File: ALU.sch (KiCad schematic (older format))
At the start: 34 parts, among them U37 74LS245, U38 74LS00, U39 74LS86, U40 74LS86, U41 74LS86, U42 74LS00, U43 74LS86, U44 74HC02, U45 74LS00, U46 74LS00, U47 74LS283, U48 74LS85, U49 74LS283, U50 74LS245, U51 74LS85, U52 74LS245, U53 74LS283, U54 74LS85, U55 74LS173, U56 74LS283, U57 74LS245, U58 74LS85

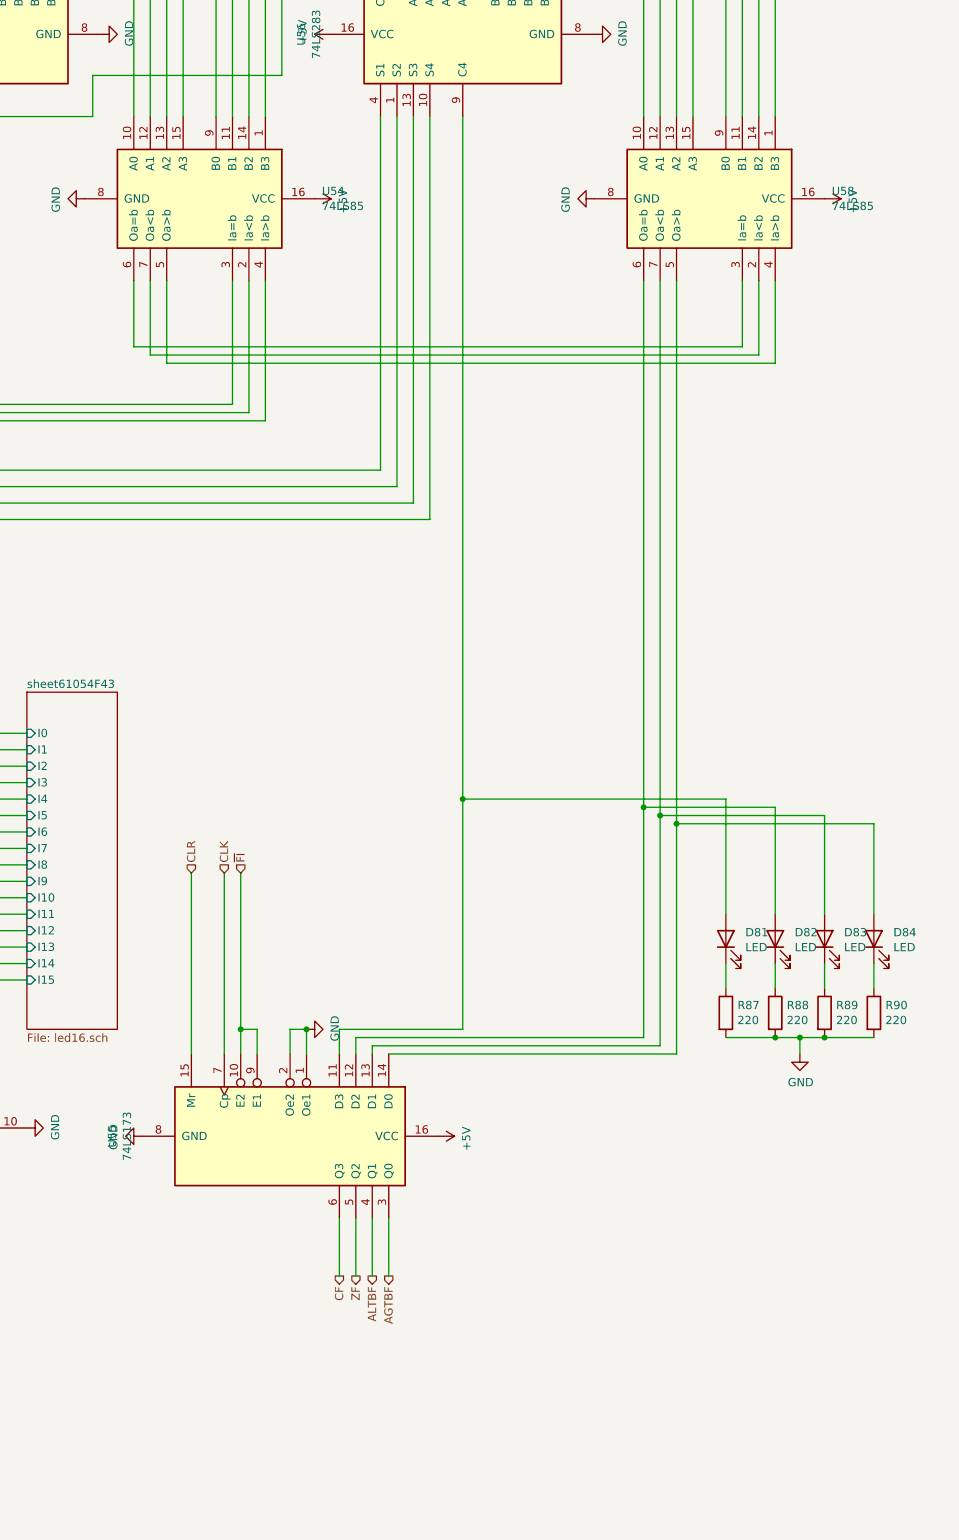
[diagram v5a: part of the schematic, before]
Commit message: added swp_x, and cleanup readme
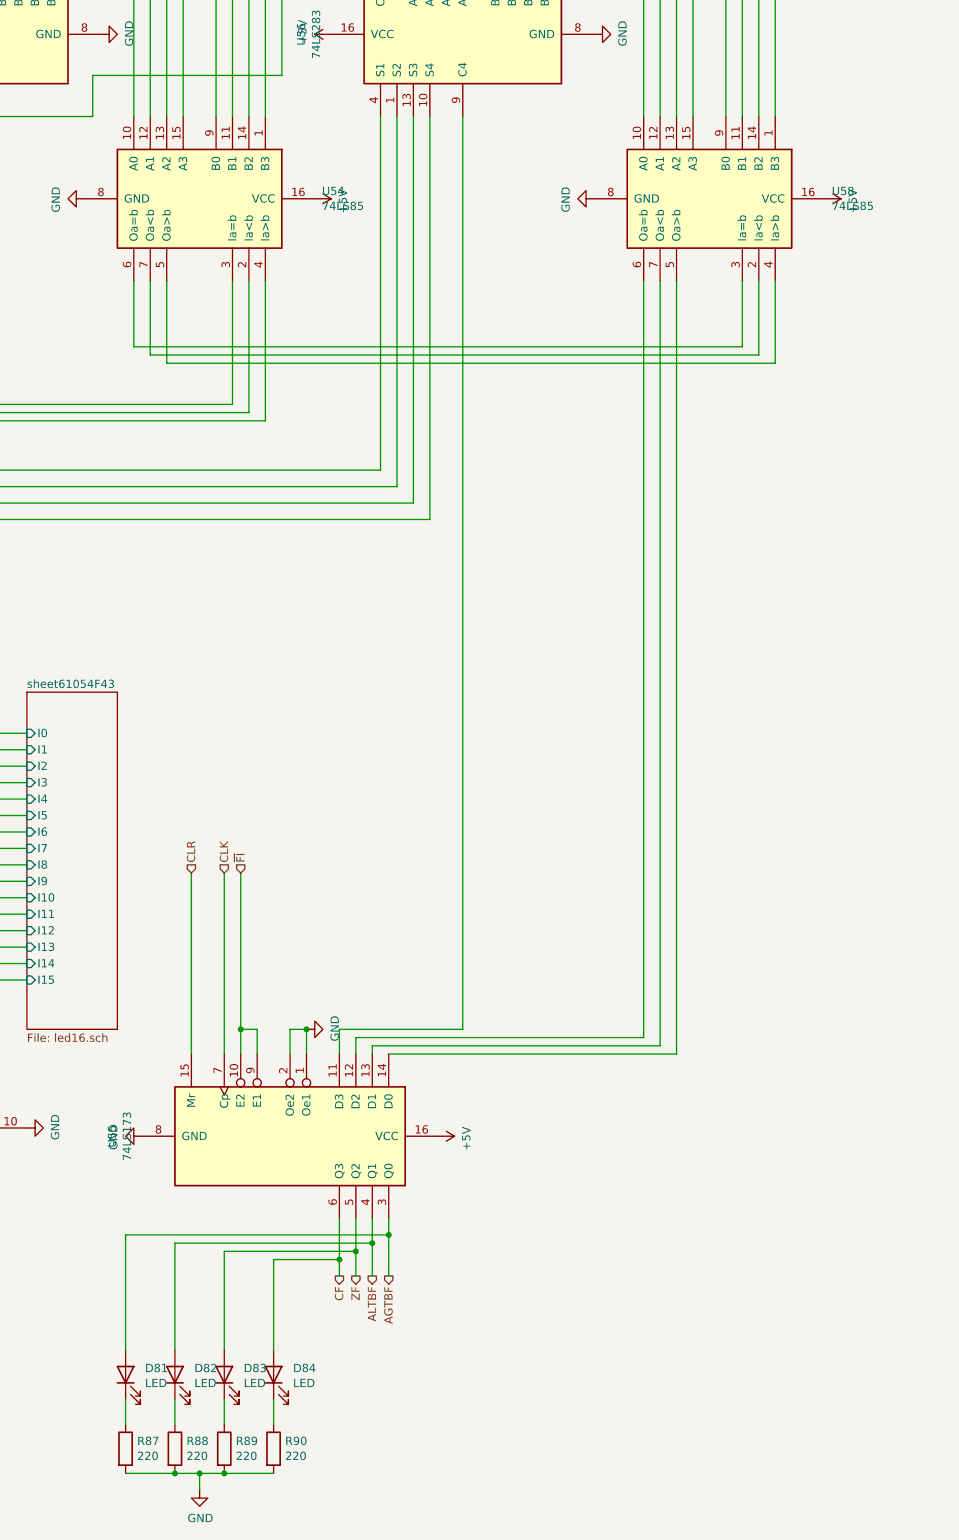
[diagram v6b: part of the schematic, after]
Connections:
- net AGTBF: now also D81.2 (A)
- net ALTBF: now also D82.2 (A)
- net CF: now also D84.2 (A)
- net ZF: now also D83.2 (A)
- net at U55.11 (D3), U56.9 (C4): no longer D81.2 (A)
- net at U55.12 (D2), U58.6 (Oa=b): no longer D82.2 (A)
- net at U55.13 (D1), U58.7 (Oa<b): no longer D83.2 (A)
- net at U55.14 (D0), U58.5 (Oa>b): no longer D84.2 (A)
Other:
- moved on the sheet: D81, D82, D83, D84, R87, R88, R89, R90
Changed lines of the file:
@@
 	17900 17350 19650 17350
 Wire Wire Line
-	19550 12650 19550 15900
-Wire Wire Line
 	19550 17300 17800 17300
 Wire Wire Line
@@
 Wire Wire Line
 	17700 17250 19450 17250
-Wire Wire Line
-	19450 17250 19450 15850
-Wire Wire Line
-	18350 11650 18350 15800
 Wire Wire Line
 	18350 17200 17600 17200
@@
 L Device:LED D?
 U 1 1 6367F2BC
-P 20250 16650
+P 16600 19300
 AR Path="/5F926C74/6367F2BC" Ref="D?"  Part="1"
 AR Path="/61968B9B/60C9B37A/6367F2BC" Ref="D?"  Part="1"
@@
 AR Path="/5FD099BF/625B6FDA/6367F2BC" Ref="D?"  Part="1"
 AR Path="/5F5F4A69/6367F2BC" Ref="D82"  Part="1"
-F 0 "D82" V 20289 16532 50  0000 R CNN
-F 1 "LED" V 20198 16532 50  0000 R CNN
-F 2 "LED_THT:LED_D3.0mm" H 20250 16650 50  0001 C CNN
-F 3 "" H 20250 16650 50  0001 C CNN
-	1    20250 16650
+F 0 "D82" V 16639 19182 50  0000 R CNN
+F 1 "LED" V 16548 19182 50  0000 R CNN
+F 2 "LED_THT:LED_D3.0mm" H 16600 19300 50  0001 C CNN
+F 3 "" H 16600 19300 50  0001 C CNN
+	1    16600 19300
 	0    -1   -1   0
 $EndComp
@@
 L Device:LED D?
 U 1 1 6367F2C2
-P 20550 16650
+P 16900 19300
 AR Path="/5F926C74/6367F2C2" Ref="D?"  Part="1"
 AR Path="/61968B9B/60C9B37A/6367F2C2" Ref="D?"  Part="1"
@@
 AR Path="/5FD099BF/625B6FDA/6367F2C2" Ref="D?"  Part="1"
 AR Path="/5F5F4A69/6367F2C2" Ref="D83"  Part="1"
-F 0 "D83" V 20589 16532 50  0000 R CNN
-F 1 "LED" V 20498 16532 50  0000 R CNN
-F 2 "LED_THT:LED_D3.0mm" H 20550 16650 50  0001 C CNN
-F 3 "" H 20550 16650 50  0001 C CNN
-	1    20550 16650
+F 0 "D83" V 16939 19182 50  0000 R CNN
+F 1 "LED" V 16848 19182 50  0000 R CNN
+F 2 "LED_THT:LED_D3.0mm" H 16900 19300 50  0001 C CNN
+F 3 "" H 16900 19300 50  0001 C CNN
+	1    16900 19300
 	0    -1   -1   0
 $EndComp
@@
 L Device:LED D?
 U 1 1 6367F2C8
-P 20850 16650
+P 17200 19300
 AR Path="/5F926C74/6367F2C8" Ref="D?"  Part="1"
 AR Path="/61968B9B/60C9B37A/6367F2C8" Ref="D?"  Part="1"
@@
 AR Path="/5FD099BF/625B6FDA/6367F2C8" Ref="D?"  Part="1"
 AR Path="/5F5F4A69/6367F2C8" Ref="D84"  Part="1"
-F 0 "D84" V 20889 16532 50  0000 R CNN
-F 1 "LED" V 20798 16532 50  0000 R CNN
-F 2 "LED_THT:LED_D3.0mm" H 20850 16650 50  0001 C CNN
-F 3 "" H 20850 16650 50  0001 C CNN
-	1    20850 16650
+F 0 "D84" V 17239 19182 50  0000 R CNN
+F 1 "LED" V 17148 19182 50  0000 R CNN
+F 2 "LED_THT:LED_D3.0mm" H 17200 19300 50  0001 C CNN
+F 3 "" H 17200 19300 50  0001 C CNN
+	1    17200 19300
 	0    -1   -1   0
 $EndComp
 Wire Wire Line
-	20250 16800 20250 16950
-Wire Wire Line
-	20550 16800 20550 16950
-Wire Wire Line
-	20850 16800 20850 16950
+	16600 19450 16600 19600
+Wire Wire Line
+	16900 19450 16900 19600
+Wire Wire Line
+	17200 19450 17200 19600
 $Comp
 L Device:R R?
 U 1 1 6367F2D7
-P 20250 17100
+P 16600 19750
 AR Path="/5F926C74/6367F2D7" Ref="R?"  Part="1"
 AR Path="/61968B9B/60C9B37A/6367F2D7" Ref="R?"  Part="1"
@@
 AR Path="/5FD099BF/625B6FDA/6367F2D7" Ref="R?"  Part="1"
 AR Path="/5F5F4A69/6367F2D7" Ref="R88"  Part="1"
-F 0 "R88" H 20320 17146 50  0000 L CNN
-F 1 "220" H 20320 17055 50  0000 L CNN
-F 2 "Resistor_THT:R_Axial_DIN0204_L3.6mm_D1.6mm_P7.62mm_Horizontal" V 20180 17100 50  0001 C CNN
-F 3 "" H 20250 17100 50  0001 C CNN
-	1    20250 17100
+F 0 "R88" H 16670 19796 50  0000 L CNN
+F 1 "220" H 16670 19705 50  0000 L CNN
+F 2 "Resistor_THT:R_Axial_DIN0204_L3.6mm_D1.6mm_P7.62mm_Horizontal" V 16530 19750 50  0001 C CNN
+F 3 "" H 16600 19750 50  0001 C CNN
+	1    16600 19750
 	1    0    0    -1
 $EndComp
@@
 L Device:R R?
 U 1 1 6367F2DD
-P 20550 17100
+P 16900 19750
 AR Path="/5F926C74/6367F2DD" Ref="R?"  Part="1"
 AR Path="/61968B9B/60C9B37A/6367F2DD" Ref="R?"  Part="1"
@@
 AR Path="/5FD099BF/625B6FDA/6367F2DD" Ref="R?"  Part="1"
 AR Path="/5F5F4A69/6367F2DD" Ref="R89"  Part="1"
-F 0 "R89" H 20620 17146 50  0000 L CNN
-F 1 "220" H 20620 17055 50  0000 L CNN
-F 2 "Resistor_THT:R_Axial_DIN0204_L3.6mm_D1.6mm_P7.62mm_Horizontal" V 20480 17100 50  0001 C CNN
-F 3 "" H 20550 17100 50  0001 C CNN
-	1    20550 17100
+F 0 "R89" H 16970 19796 50  0000 L CNN
+F 1 "220" H 16970 19705 50  0000 L CNN
+F 2 "Resistor_THT:R_Axial_DIN0204_L3.6mm_D1.6mm_P7.62mm_Horizontal" V 16830 19750 50  0001 C CNN
+F 3 "" H 16900 19750 50  0001 C CNN
+	1    16900 19750
 	1    0    0    -1
 $EndComp
@@
 L Device:R R?
 U 1 1 6367F2E3
-P 20850 17100
+P 17200 19750
 AR Path="/5F926C74/6367F2E3" Ref="R?"  Part="1"
 AR Path="/61968B9B/60C9B37A/6367F2E3" Ref="R?"  Part="1"
@@
 AR Path="/5FD099BF/625B6FDA/6367F2E3" Ref="R?"  Part="1"
 AR Path="/5F5F4A69/6367F2E3" Ref="R90"  Part="1"
-F 0 "R90" H 20920 17146 50  0000 L CNN
-F 1 "220" H 20920 17055 50  0000 L CNN
-F 2 "Resistor_THT:R_Axial_DIN0204_L3.6mm_D1.6mm_P7.62mm_Horizontal" V 20780 17100 50  0001 C CNN
-F 3 "" H 20850 17100 50  0001 C CNN
-	1    20850 17100
-	1    0    0    -1
-$EndComp
-Wire Wire Line
-	19950 17250 20250 17250
-Connection ~ 20250 17250
-Wire Wire Line
-	20250 17250 20400 17250
-Connection ~ 20550 17250
-Wire Wire Line
-	20550 17250 20850 17250
+F 0 "R90" H 17270 19796 50  0000 L CNN
+F 1 "220" H 17270 19705 50  0000 L CNN
+F 2 "Resistor_THT:R_Axial_DIN0204_L3.6mm_D1.6mm_P7.62mm_Horizontal" V 17130 19750 50  0001 C CNN
+F 3 "" H 17200 19750 50  0001 C CNN
+	1    17200 19750
+	1    0    0    -1
+$EndComp
+Wire Wire Line
+	16300 19900 16600 19900
+Connection ~ 16600 19900
+Wire Wire Line
+	16600 19900 16750 19900
+Connection ~ 16900 19900
+Wire Wire Line
+	16900 19900 17200 19900
 $Comp
 L Device:LED D?
 U 1 1 636C3FB6
-P 19950 16650
+P 16300 19300
 AR Path="/5F926C74/636C3FB6" Ref="D?"  Part="1"
 AR Path="/61968B9B/60C9B37A/636C3FB6" Ref="D?"  Part="1"
@@
 AR Path="/5FD099BF/625B6FDA/636C3FB6" Ref="D?"  Part="1"
 AR Path="/5F5F4A69/636C3FB6" Ref="D81"  Part="1"
-F 0 "D81" V 19989 16532 50  0000 R CNN
-F 1 "LED" V 19898 16532 50  0000 R CNN
-F 2 "LED_THT:LED_D3.0mm" H 19950 16650 50  0001 C CNN
-F 3 "" H 19950 16650 50  0001 C CNN
-	1    19950 16650
+F 0 "D81" V 16339 19182 50  0000 R CNN
+F 1 "LED" V 16248 19182 50  0000 R CNN
+F 2 "LED_THT:LED_D3.0mm" H 16300 19300 50  0001 C CNN
+F 3 "" H 16300 19300 50  0001 C CNN
+	1    16300 19300
 	0    -1   -1   0
 $EndComp
 Wire Wire Line
-	19950 16800 19950 16950
+	16300 19450 16300 19600
 $Comp
 L Device:R R?
 U 1 1 636C3FBF
-P 19950 17100
+P 16300 19750
 AR Path="/5F926C74/636C3FBF" Ref="R?"  Part="1"
 AR Path="/61968B9B/60C9B37A/636C3FBF" Ref="R?"  Part="1"
@@
 AR Path="/5FD099BF/625B6FDA/636C3FBF" Ref="R?"  Part="1"
 AR Path="/5F5F4A69/636C3FBF" Ref="R87"  Part="1"
-F 0 "R87" H 20020 17146 50  0000 L CNN
-F 1 "220" H 20020 17055 50  0000 L CNN
-F 2 "Resistor_THT:R_Axial_DIN0204_L3.6mm_D1.6mm_P7.62mm_Horizontal" V 19880 17100 50  0001 C CNN
-F 3 "" H 19950 17100 50  0001 C CNN
-	1    19950 17100
-	1    0    0    -1
-$EndComp
-Wire Wire Line
-	20850 15950 20850 16500
-Wire Wire Line
-	20550 15900 20550 16500
-Wire Wire Line
-	20250 15850 20250 16500
-Wire Wire Line
-	19950 15800 19950 16500
+F 0 "R87" H 16370 19796 50  0000 L CNN
+F 1 "220" H 16370 19705 50  0000 L CNN
+F 2 "Resistor_THT:R_Axial_DIN0204_L3.6mm_D1.6mm_P7.62mm_Horizontal" V 16230 19750 50  0001 C CNN
+F 3 "" H 16300 19750 50  0001 C CNN
+	1    16300 19750
+	1    0    0    -1
+$EndComp
+Wire Wire Line
+	17200 18600 17200 19150
+Wire Wire Line
+	16900 18550 16900 19150
+Wire Wire Line
+	16600 18500 16600 19150
+Wire Wire Line
+	16300 18450 16300 19150
 $Comp
 L 16bitCpu-rescue:GND-power #PWR?
 U 1 1 6385D433
-P 20400 17350
+P 16750 20000
 AR Path="/6385D433" Ref="#PWR?"  Part="1"
 AR Path="/5F5F4A69/6385D433" Ref="#PWR0168"  Part="1"
-F 0 "#PWR0168" H 20400 17100 50  0001 C CNN
-F 1 "GND" H 20405 17177 50  0000 C CNN
-F 2 "" H 20400 17350 50  0001 C CNN
-F 3 "" H 20400 17350 50  0001 C CNN
-	1    20400 17350
-	1    0    0    -1
-$EndComp
-Wire Wire Line
-	20400 17250 20400 17350
-Connection ~ 20400 17250
-Wire Wire Line
-	20400 17250 20550 17250
+F 0 "#PWR0168" H 16750 19750 50  0001 C CNN
+F 1 "GND" H 16755 19827 50  0000 C CNN
+F 2 "" H 16750 20000 50  0001 C CNN
+F 3 "" H 16750 20000 50  0001 C CNN
+	1    16750 20000
+	1    0    0    -1
+$EndComp
+Wire Wire Line
+	16750 19900 16750 20000
+Connection ~ 16750 19900
+Wire Wire Line
+	16750 19900 16900 19900
 Wire Wire Line
 	8250 2800 8250 6050
@@
 	3650 2200 3650 6700
 Wire Wire Line
-	17700 18350 17700 18700
-Wire Wire Line
-	17600 18350 17600 18700
-Wire Wire Line
-	17800 18350 17800 18700
-Wire Wire Line
-	17900 18350 17900 18700
-Wire Wire Line
-	20850 15950 19650 15950
-Wire Wire Line
-	19650 12650 19650 15950
-Connection ~ 19650 15950
-Wire Wire Line
-	19650 15950 19650 17350
-Wire Wire Line
-	20550 15900 19550 15900
-Connection ~ 19550 15900
-Wire Wire Line
-	19550 15900 19550 17300
-Wire Wire Line
-	20250 15850 19450 15850
-Connection ~ 19450 15850
-Wire Wire Line
-	19450 15850 19450 12650
-Wire Wire Line
-	19950 15800 18350 15800
-Connection ~ 18350 15800
-Wire Wire Line
-	18350 15800 18350 17200
+	17700 18350 17700 18550
+Wire Wire Line
+	17600 18350 17600 18600
+Wire Wire Line
+	17800 18350 17800 18500
+Wire Wire Line
+	17900 18350 17900 18450
 Wire Wire Line
 	14050 13250 14050 12650
@@
 	1    0    0    -1
 $EndComp
+Wire Wire Line
+	19550 12650 19550 17300
+Wire Wire Line
+	19450 12650 19450 17250
+Wire Wire Line
+	18350 11650 18350 17200
+Wire Wire Line
+	19650 12650 19650 17350
+Wire Wire Line
+	17200 18600 17600 18600
+Connection ~ 17600 18600
+Wire Wire Line
+	17600 18600 17600 18700
+Wire Wire Line
+	16900 18550 17700 18550
+Connection ~ 17700 18550
+Wire Wire Line
+	17700 18550 17700 18700
+Wire Wire Line
+	16600 18500 17800 18500
+Connection ~ 17800 18500
+Wire Wire Line
+	17800 18500 17800 18700
+Wire Wire Line
+	16300 18450 17900 18450
+Connection ~ 17900 18450
+Wire Wire Line
+	17900 18450 17900 18700
 $EndSCHEMATC

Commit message: clean up
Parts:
- renumbered U37 to U39, U38 to U40, U39 to U41, U40 to U42, U41 to U43, U42 to U44, U43 to U45, U44 to U46, U45 to U47, U46 to U48, U47 to U49, U48 to U50, U49 to U51, U50 to U52, U51 to U53, U52 to U54, U53 to U55, U54 to U56, U55 to U57, U56 to U58, U57 to U59, U58 to U60
